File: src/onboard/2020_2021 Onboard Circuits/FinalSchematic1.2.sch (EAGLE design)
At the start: 93 parts, among them IC1 A5975D, IC2 A5975D, IC3 A5975D

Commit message: Updated board using the jlcpcb2layer.dru file for DRC check. Added names next to pinheaders. Adjusted silkscreen of component names. Updated photos of baord and schematic.
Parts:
- removed 3: (no value), pinhead:PINHD-1X4
- added JP1: (no value), pinhead:PINHD-1X3
- added R1: 1.8M, adafruit:R-US_0204/7
- added R18: 430k, adafruit:R-US_0204/7
- renumbered DIP1 to DIP_1_2, DIP2 to DIP_3_4, DIP3 to LEDBANK2, DIP4 to LEDBANK1
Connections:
- net 22_INPUT: now also R1.2
- net GND: now also R18.1
- net PIN13: now also JP1.3; no longer 3.4
- net PIN14: now also R1.1, R18.2; no longer 3.3
- net PIN16: now also JP1.2; no longer 3.2
- net PIN17: now also JP1.1; no longer 3.1
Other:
- note added: "Battery Level"

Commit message: Added button connection, rewired radio, removed pitot tube, split into pages
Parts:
- removed 1, 2, 5: (no value), pinhead:PINHD-1X2
- removed 4: (no value), pinhead:PINHD-1X5
- removed DIP_1_2, DIP_3_4, JP1, LEDBANK1, LEDBANK2: (no value), pinhead:PINHD-1X3
- removed PITOT_TUBE: (no value), con-lstb:MA03-1
- removed PTR1: 2.2K, adafruit:R-US_0204/7
- removed PTR2: 4.3K, adafruit:R-US_0204/7
- added BTNBANK: (no value), adafruit:PINHD-1X3
- added DIPBANK, LEDBANK: (no value), adafruit:PINHD-1X6
- added R19, R22: 2.2k, adafruit:R-US_0204/7
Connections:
- removed net MOSI1: RADIO.MOSI, TEENSY4.1.26-A12/MOSI1
- removed net N$4: PITOT_TUBE.1, PTR1.2
- removed net PIN0: 2.2, TEENSY4.1.0-RX1/CS1/CRX2
- removed net PIN1: 2.1, TEENSY4.1.1-TX1/MISO1/CTX2
- removed net PIN10: 4.5, TEENSY4.1.10-CS/MQSR
- removed net PIN11: 4.4, TEENSY4.1.11-MOSI/CTX1
- removed net PIN12: 4.3, TEENSY4.1.12-MISO/MQSL
- removed net PIN13: JP1.3, TEENSY4.1.13-SCK/LED
- removed net PIN14: R1.1, R18.2, TEENSY4.1.14-A0/TX3/SPDIF_OUT
- removed net PIN16: JP1.2, TEENSY4.1.16-A2/RX4/SCL1
- removed net PIN17: JP1.1, TEENSY4.1.17-A3/TX4/SDA1
- removed net PIN24: 4.2, TEENSY4.1.24-A10/TX6/SCL2
- removed net PIN25: 4.1, TEENSY4.1.25-A11/RX6/SDA2
- removed net PIN29: 1.2, TEENSY4.1.29-TX7
- removed net PIN31: 1.1, TEENSY4.1.31-CTX3
- removed net PIN5: 5.2, TEENSY4.1.5-IN2
- removed net PIN6: 5.1, TEENSY4.1.6-OUT1D
- removed net PT_ANLGPIN: PTR1.1, PTR2.2, TEENSY4.1.39-A15/CS/OUT1A
- removed net RADIO_CS: RADIO.CS, TEENSY4.1.38-A14/CS/IN1
- removed net SCK1: RADIO.SCK, TEENSY4.1.27-A13/SCK1
- new net BATLEVEL: R1.1, R18.2
- new net CS0: RADIO.CS, TEENSY4.1.10-CS/MQSR
- new net MISO0: RADIO.MISO, TEENSY4.1.12-MISO/MQSL
- new net MOSI0: RADIO.MOSI, TEENSY4.1.11-MOSI/CTX1
- new net N$3: BTNBANK.1, R22.2
- new net N$5: BTNBANK.2, R19.2
- new net SCK0: RADIO.SCK, TEENSY4.1.13-SCK/LED
- net 3.3V: now also TEENSY4.1.3V3-2
- net 5V: now also BTNBANK.3, DIPBANK.6, R33.2; no longer DIP_1_2.3, PITOT_TUBE.3, R33.1
- net BLUE: now also LEDBANK.5; no longer LEDBANK2.2
- net DIP1: now also DIPBANK.5; no longer DIP_1_2.2
- net DIP2: now also DIPBANK.4; no longer DIP_1_2.1
- net DIP3: now also DIPBANK.3; no longer DIP_3_4.3
- net DIP4: now also DIPBANK.2; no longer DIP_3_4.2
- net GND: now also DIPBANK.1, R19.1, R22.1, TEENSY4.1.GND2, TEENSY4.1.GND4, TEENSY4.1.GND5; no longer DIP_3_4.1, PITOT_TUBE.2, PTR2.1
- net GNDADDRESS: no longer R21.2
- net GREEN: now also LEDBANK.6; no longer LEDBANK2.3
- net MISO1: no longer RADIO.MISO
- net ORANGE: now also LEDBANK.1; no longer LEDBANK1.1
- net RADIO_RST: now also TEENSY4.1.6-OUT1D; no longer TEENSY4.1.28-RX7
- net RED: now also LEDBANK.4; no longer LEDBANK2.1
- net SCL: now also R32.1; no longer R33.2
- net SDA: now also R33.1; no longer R32.1
- net WHITE: now also LEDBANK.2; no longer LEDBANK1.2
- net YELLOW: now also LEDBANK.3; no longer LEDBANK1.3
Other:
- note removed: "Battery Level"

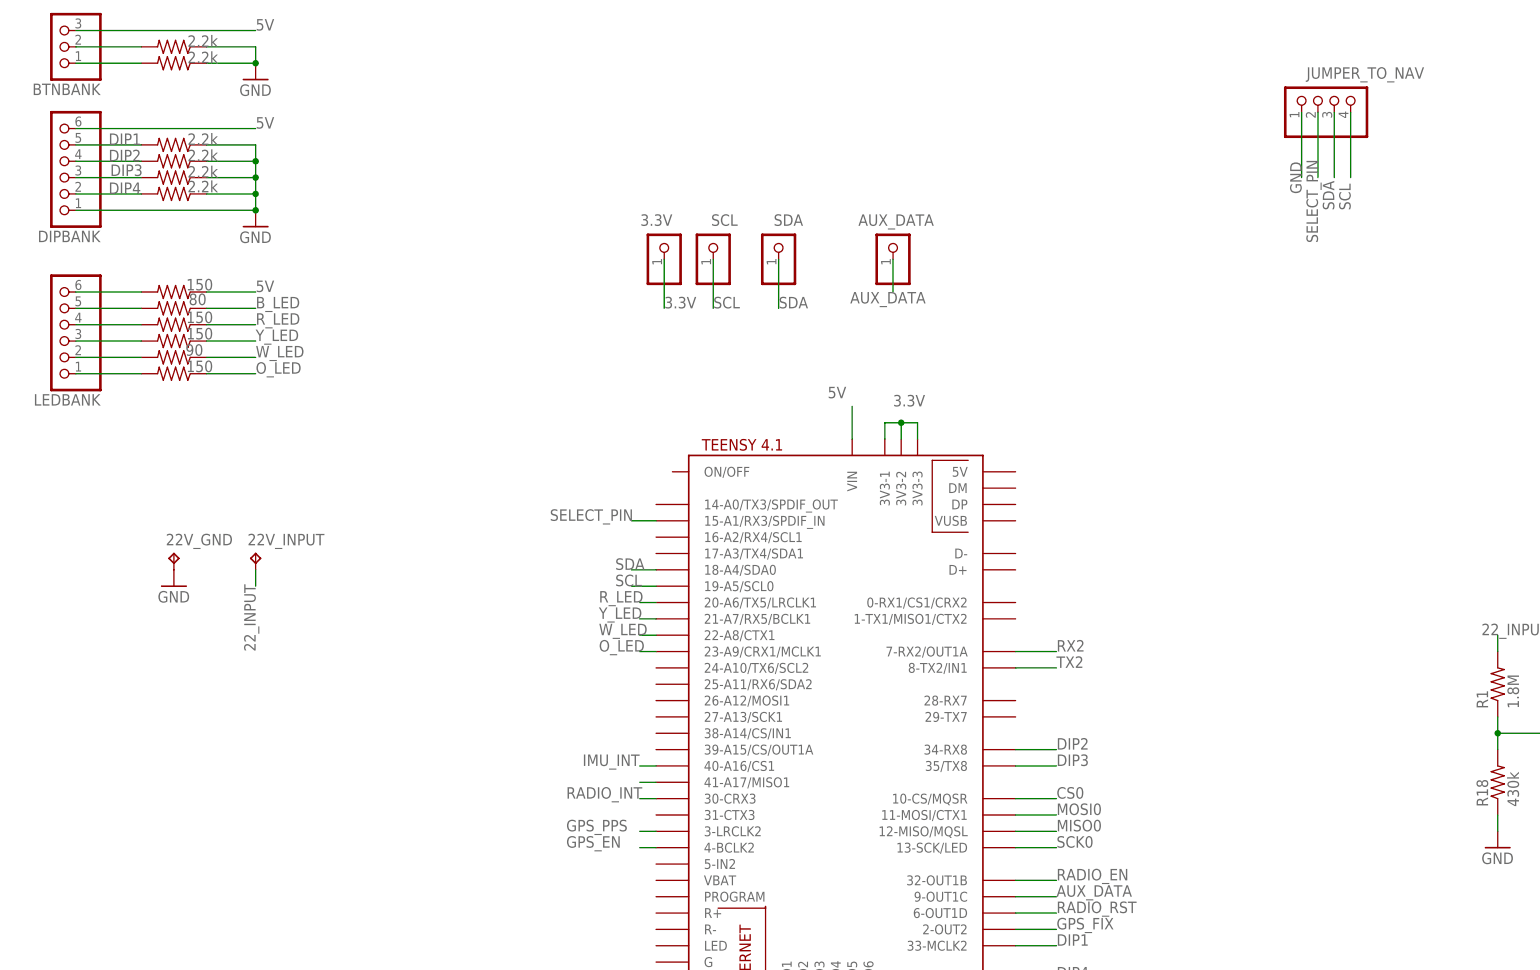
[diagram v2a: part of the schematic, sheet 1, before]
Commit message: Added 5v connector
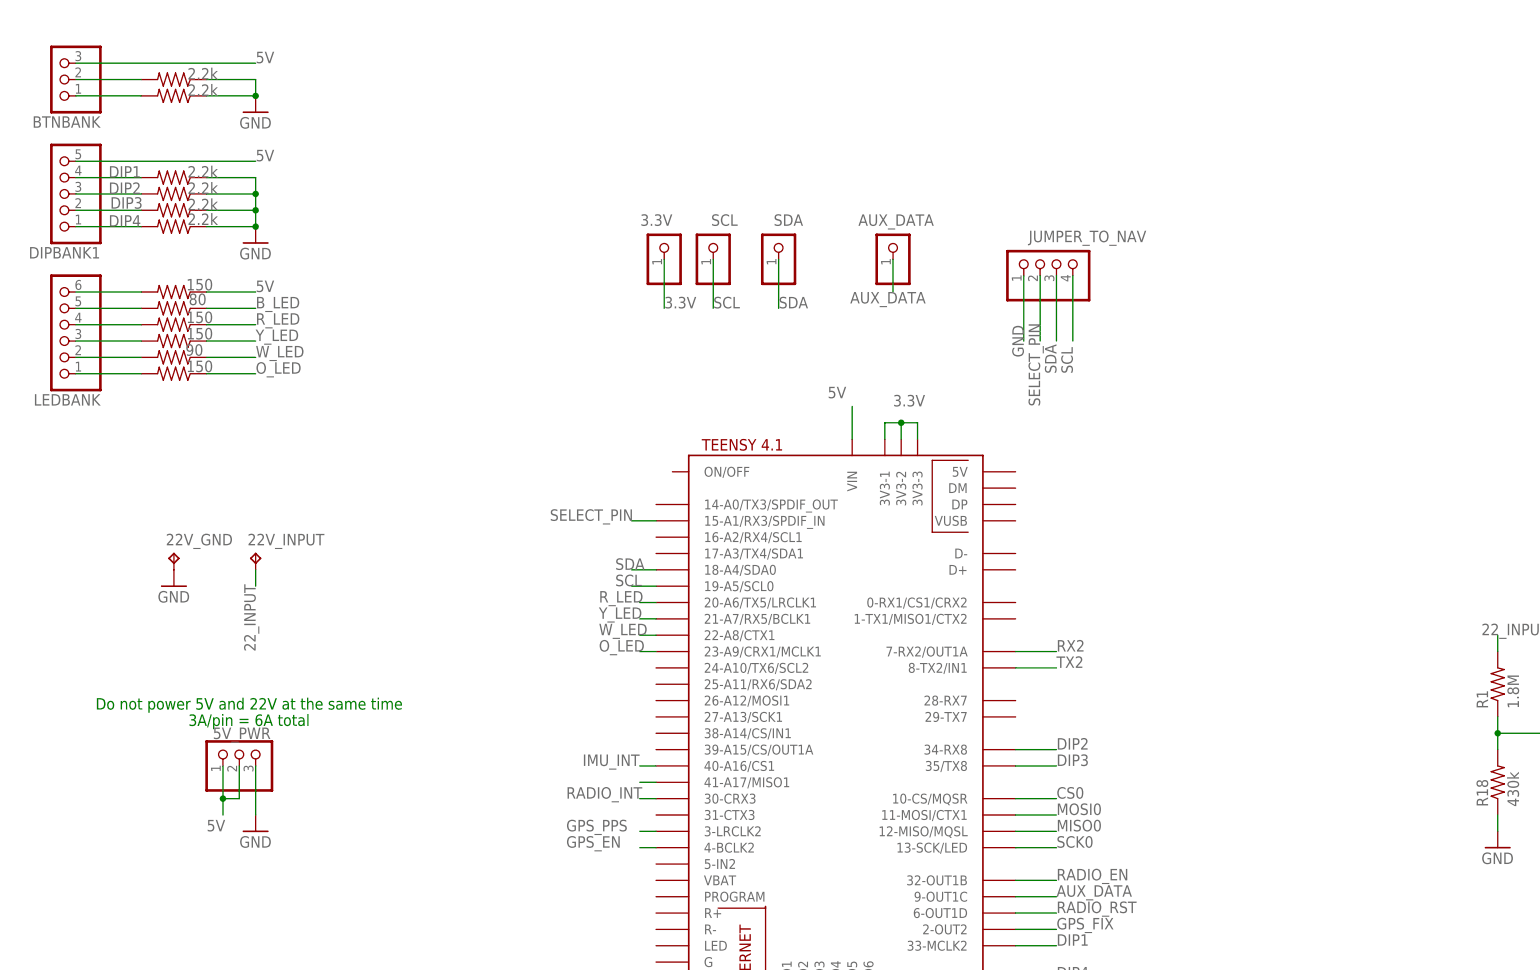
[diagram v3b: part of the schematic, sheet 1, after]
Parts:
- removed DIPBANK: (no value), adafruit:PINHD-1X6
- added 5V_PWR: (no value), pinhead:PINHD-1X3
- added DIPBANK1: (no value), pinhead:PINHD-1X5
- BTNBANK: device adafruit:PINHD-1X3 -> pinhead:PINHD-1X3
- LEDBANK: device adafruit:PINHD-1X6 -> pinhead:PINHD-1X6
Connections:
- net 5V: now also 5V_PWR.1, 5V_PWR.2, DIPBANK1.5; no longer DIPBANK.6
- net DIP1: now also DIPBANK1.4; no longer DIPBANK.5
- net DIP2: now also DIPBANK1.3; no longer DIPBANK.4
- net DIP3: now also DIPBANK1.2; no longer DIPBANK.3
- net DIP4: now also DIPBANK1.1; no longer DIPBANK.2
- net GND: now also 5V_PWR.3; no longer DIPBANK.1
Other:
- note added: "3A/pin = 6A total"
- note added: "Do not power 5V and 22V at the same time"
- moved on the sheet: BTNBANK, JUMPER_TO_NAV

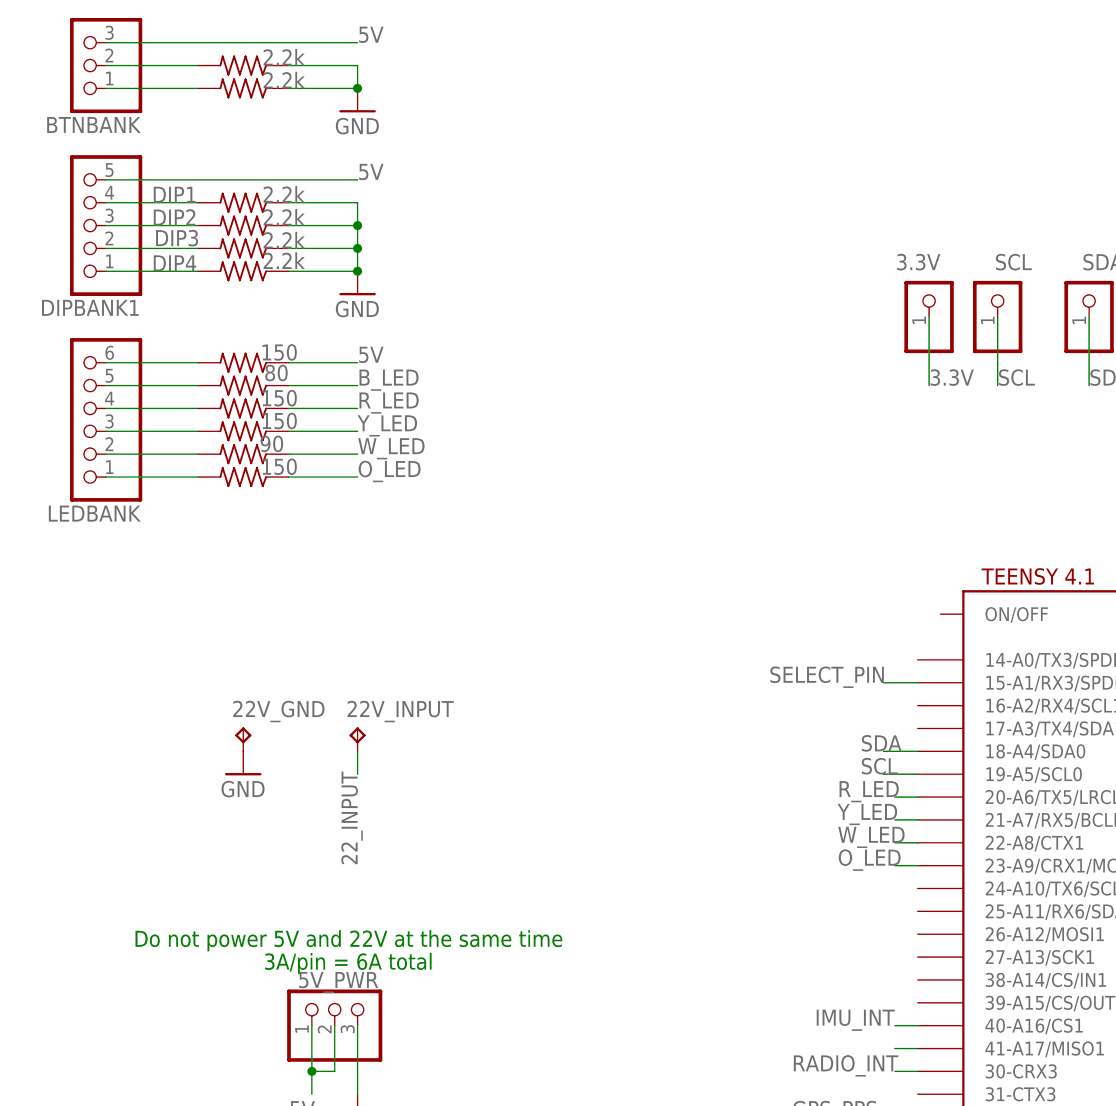
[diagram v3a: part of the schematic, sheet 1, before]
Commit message: Added button wires and fixed 5v input
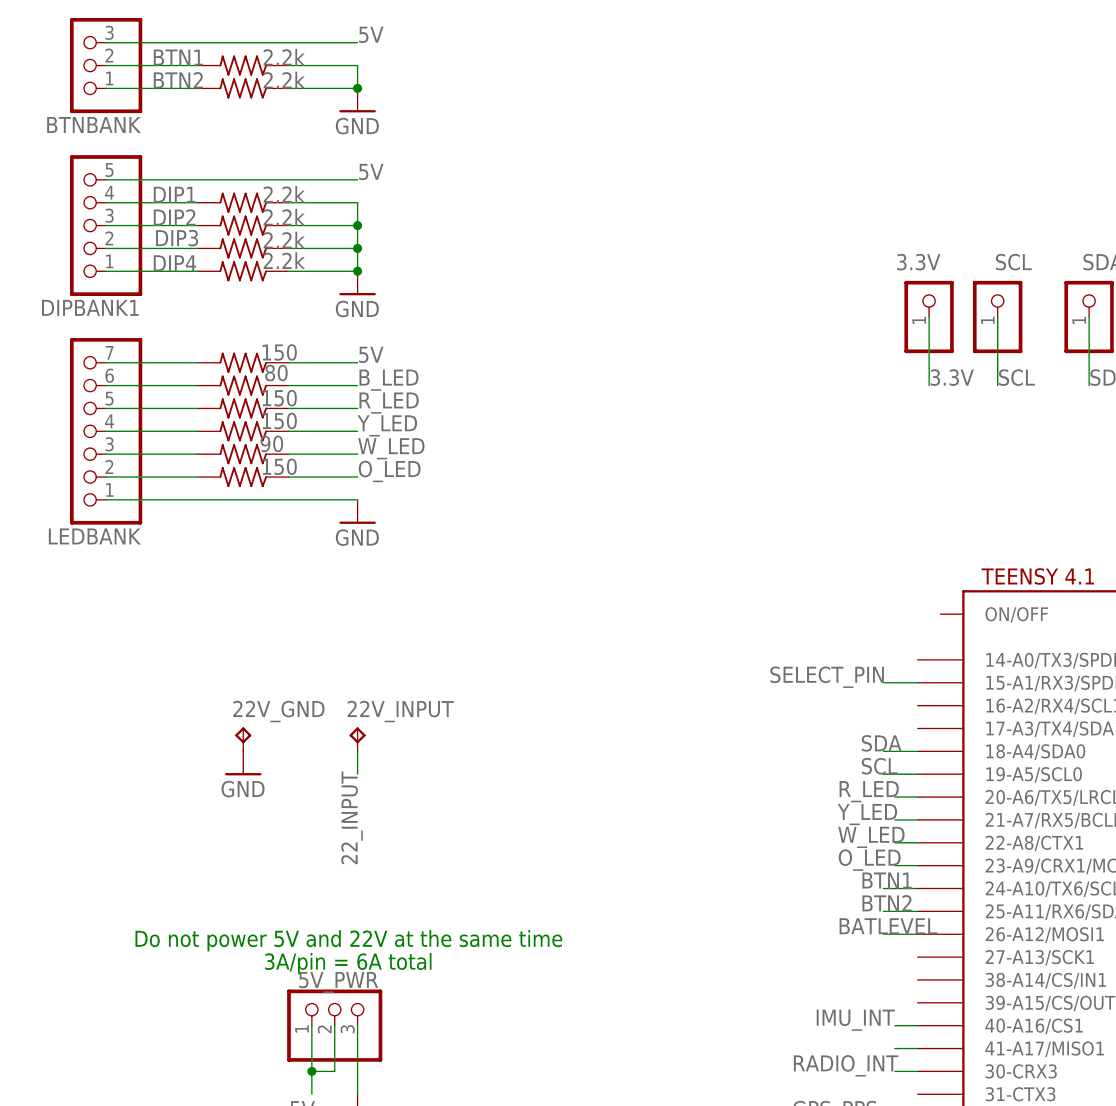
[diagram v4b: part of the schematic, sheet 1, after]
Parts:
- LEDBANK: device pinhead:PINHD-1X6 -> pinhead:PINHD-1X7
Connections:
- removed net N$3: BTNBANK.1, R22.2
- removed net N$5: BTNBANK.2, R19.2
- new net BTN1: BTNBANK.2, R19.2, TEENSY4.1.24-A10/TX6/SCL2
- new net BTN2: BTNBANK.1, R22.2, TEENSY4.1.25-A11/RX6/SDA2
- net 5V: now also SV1.2, SV10.2, SV11.2, SV12.2, SV13.2, SV14.2, SV15.2, SV16.2, SV2.2, SV3.2, SV4.2, SV5.2, SV6.2, SV7.2, SV8.2, SV9.2
- net BATLEVEL: now also TEENSY4.1.26-A12/MOSI1
- net BLUE: now also LEDBANK.6; no longer LEDBANK.5
- net GND: now also LEDBANK.1
- net GNDADDRESS: now also R21.2
- net GREEN: now also LEDBANK.7; no longer LEDBANK.6
- net ORANGE: now also LEDBANK.2; no longer LEDBANK.1
- net OUTPUT_BUCK1: no longer SV1.2, SV10.2, SV12.2, SV13.2, SV14.2, SV15.2, SV7.2, SV8.2
- net OUTPUT_BUCK2: no longer SV11.2, SV16.2, SV2.2, SV3.2, SV4.2, SV5.2, SV6.2, SV9.2
- net RED: now also LEDBANK.5; no longer LEDBANK.4
- net WHITE: now also LEDBANK.3; no longer LEDBANK.2
- net YELLOW: now also LEDBANK.4; no longer LEDBANK.3

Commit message: Added 6v->5v LDO regulator
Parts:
- removed 22V_GND, 22V_INPUT: TPPAD1-17Y, testpad:TPPAD1-17Y
- removed 3.3V, 5V, 6V1, 6V2, SCL, SDA: (no value), pinhead:PINHD-1X1
- removed C11, C13: 470uF, capacitor-wima:C2,5-3
- removed C2: 10uF, capacitor-wima:C2,5-3
- removed IC2: A5975D, A5975D:A5975D
- removed L1, L6: 27uH, rcl:L-USTFI0307
- removed R24, R51: 1.5k, adafruit:R-US_0204/7
- removed R25, R50: 5.6k, adafruit:R-US_0204/7
- added 22V_PWR, 6V_PWR: (no value), pinhead:PINHD-1X3
- added TP1, TP2, TP3, TP4, TP5: PTR1B1,27, testpad:PTR1B1,27
- IC1: value A5975D -> MIC2937A-5.0BT; device A5975D:A5975D -> linear:786TV
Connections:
- removed net N$12: IC2.OUT, L1.2
- removed net N$19: IC2.FB, R24.2, R25.1
- removed net N$8: IC1.OUT, L6.2
- removed net N$9: IC1.FB, R50.1, R51.2
- removed net OUTPUT_BUCK1: 6V1.1, C13.1, L6.1, R50.2
- removed net OUTPUT_BUCK2: 6V2.1, C11.1, L1.1, R25.2
- new net 22V_INPUT: 22V_PWR.1, 22V_PWR.2, C3.1, IC3.VCC, TP4.TP
- new net 6V: 6V_PWR.1, 6V_PWR.2, IC1.VI
- new net N$5: TP5.TP
- net 22_INPUT: no longer 22V_INPUT.TP, C1.1, C2.1, C3.1, IC1.VCC, IC2.VCC, IC3.VCC
- net 3.3V: no longer 3.3V.1, IC1.VREF, IC2.VREF
- net 5V: now also C1.1, IC1.VO, TP1.TP; no longer 5V.1
- net GND: now also 22V_PWR.3, 6V_PWR.3; no longer 22V_GND.TP, C1.2, C11.2, C13.2, C2.2, IC1.INH, IC2.GND, IC2.INH, R24.1, R51.1
- net SCL: now also TP3.TP; no longer SCL.1
- net SDA: now also TP2.TP; no longer SDA.1
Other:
- note added: "22V to 5V SMPS regulation"
- note added: "6V to 5V LDO regulation"
- note added: "Do not power 5V, 6V, and 22V at the same time"
- note removed: "Do not power 5V and 22V at the same time"
